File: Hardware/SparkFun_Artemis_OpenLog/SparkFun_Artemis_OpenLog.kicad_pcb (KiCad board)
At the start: 4 copper layers, 30.5 x 30.5 mm, 140 parts, among them J11 QWIIC_RIGHT_ANGLE, J14 CORTEX_JTAG, J6 MICRO-SD, Q1 20V/0.2A/8MHz/1.2Ω/1Vth, Q10 20V/0.2A/8MHz/1.2Ω/1Vth, Q2 20V/4.2A/52mΩ/1.4W, Q3 20V/0.2A/8MHz/1.2Ω/1Vth, Q7 20V/0.2A/8MHz/1.2Ω/1Vth, Q9 20V/0.2A/8MHz/1.2Ω/1Vth, U1 3.0V Supervisor, U10 CH340E, U13 9DoF IMU, U14 1.8V/100mA, U2 MCP73831, U3 3.3V, U4 3.3V, U8 ARTEMIS_MODULE, Y3 32.768kHz

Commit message: Updates the design export
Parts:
- removed C51, C52: 0.1uF, 0402-TIGHT
- removed C53, C54: 1.0uF, 0402-TIGHT
- removed Q1, Q10, Q3, Q7, Q9: 20V/0.2A/8MHz/1.2Ω/1Vth, SOT-416FL
- removed R40, R41, R44, R45, R46, R47, R48: 2.2k, 0402-TIGHT
- removed R49: DNP, 0402-TIGHT
- removed U13: 9DoF IMU, QFN24-3X3-ICM-20948
- removed U14: 1.8V/100mA, SC70
- added C10: 0.1uF, 0402, B.Cu at (161.7, 107.5)
- added C11: 0.1uF, 0402, B.Cu at (161.7, 106.0)
- added C6: 22pF, 0402-TIGHT, B.Cu at (159.6, 96.9)
- added C8: 22pF, 0402-TIGHT, B.Cu at (161.7, 96.9)
- added C9: 0.1uF, 0402, B.Cu at (159.2, 106.0)
- added R10: 4.7k, 0402-TIGHT, B.Cu at (158.9, 110.6)
- added R11: 4.7k, 0402-TIGHT, B.Cu at (158.9, 109.6)
- added R12: 100k, 0402-TIGHT, B.Cu at (161.7, 95.9)
- added R9: 100k, 0402-TIGHT, B.Cu at (158.9, 108.6)
- added U5: BNO086, LGA-28, B.Cu at (159.9, 102.5)
- added Y1: 32.768kHz, CRYSTAL-SMD-3.2X1.5MM, B.Cu at (160.7, 98.4)
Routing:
- net ICM-20948-LV_#_1.8V: track 43.4 -> 0.00 mm, vias 4 -> 0
- net ICM_PWR: track 41.5 -> 0.00 mm, vias 3 -> 0
- net SCK: track 53.8 -> 25.5 mm, vias 3 -> 2
- net ICM_~{CS}: track 34.6 -> 20.2 mm
- net S_SDA: track 0.00 -> 10.2 mm
- net N$5: track 0.00 -> 8.04 mm
- net S_SCL: track 0.00 -> 7.95 mm
- net ICM_INT: track 17.7 -> 24.1 mm, vias 1 -> 3
- net ~{RST}: track 0.00 -> 6.24 mm
- net GND: track 17.3 -> 11.8 mm, vias 35 -> 29
- net ICM-20948-LV_~{CS}: track 5.56 -> 0.00 mm
- net SDO: track 32.7 -> 27.2 mm
- net ICM-20948-LV_SDO: track 5.13 -> 0.00 mm
- net N$3: track 0.00 -> 4.71 mm
- net ICM-20948-LV_SCK: track 4.65 -> 0.00 mm
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
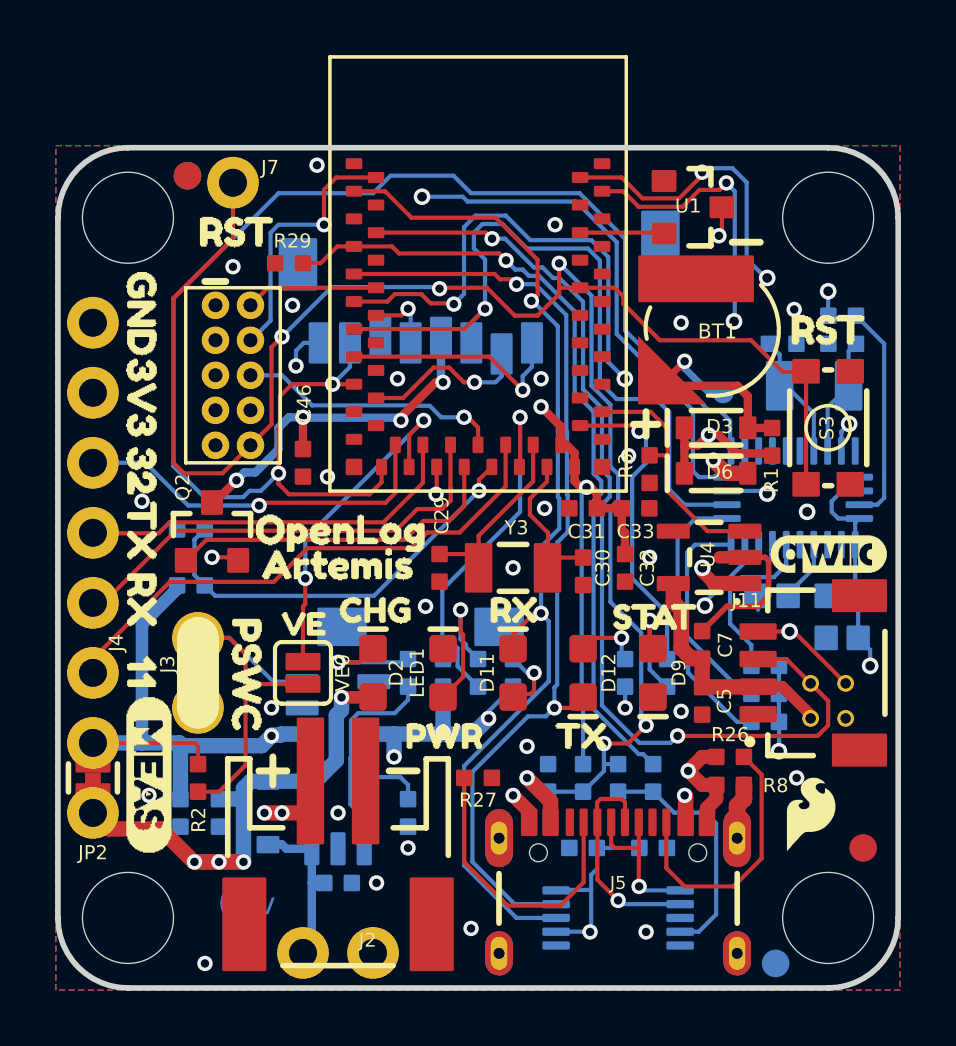
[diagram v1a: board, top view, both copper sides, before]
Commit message: Generates footprint library, updates many parts from the SparkFun KiCaad libraries
* This is just a save point
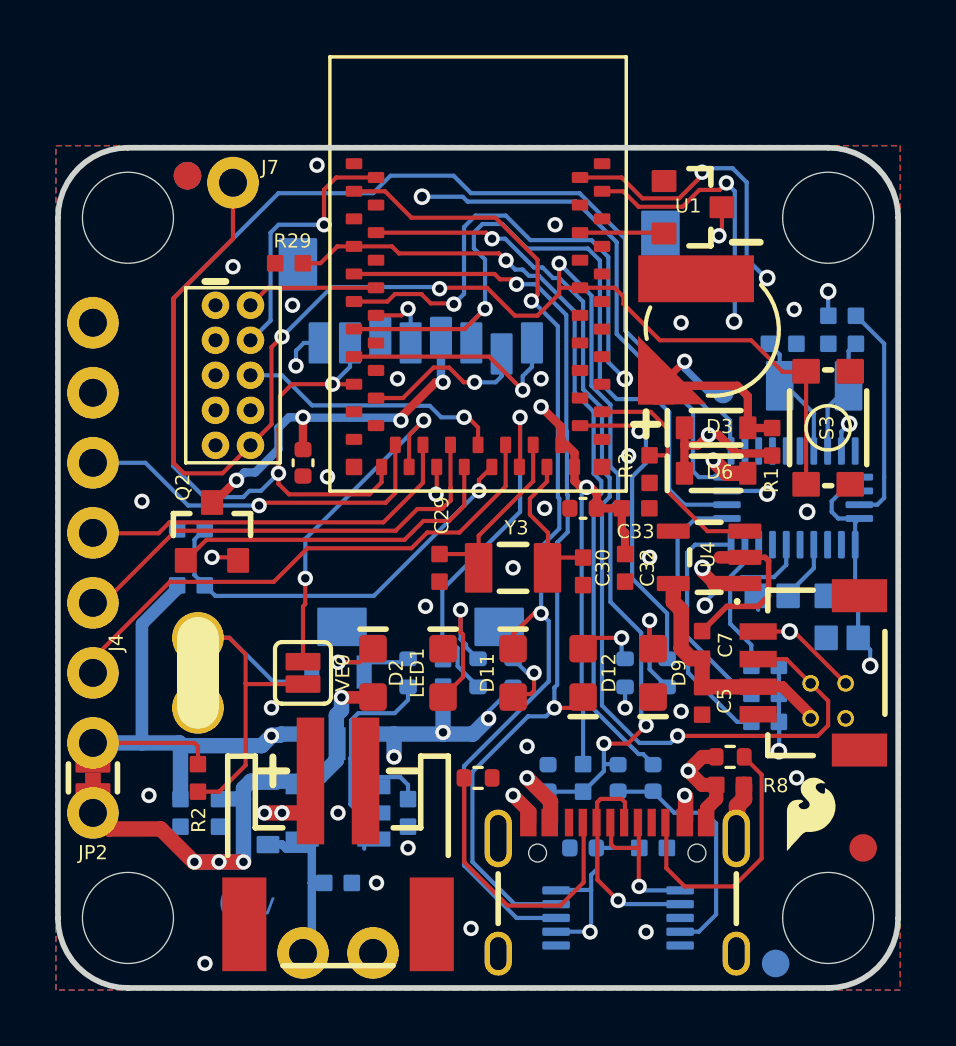
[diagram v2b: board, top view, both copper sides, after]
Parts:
- removed J1: , 1X02_NO_SILK
- removed U$1: , QWIIC#LOGO#JPG
- removed U$10, U$11: , PSWC0
- removed U$12, U$8: , RST0
- removed U$13: , C0
- removed U$14: , D0
- removed U$15: , 30
- removed U$2: , CHG2
- removed U$27: , MEAS3
- removed U$28: , OPENLOG12
- removed U$3: , PWR0
- removed U$32: , RST9
- removed U$33: , VIN8
- removed U$34, U$35: , 3V34
- removed U$36, U$37: , 113
- removed U$38, U$39: , 322
- removed U$4: , RX4
- removed U$40, U$41: , GND5
- removed U$42, U$54: , RX1
- removed U$43, U$49: , X0
- removed U$44, U$50: , Y1
- removed U$45, U$51: , Z2
- removed U$46: , G5
- removed U$47: , A4
- removed U$48: , M3
- removed U$5: , STAT5
- removed U$55, U$56: , TX0
- removed U$6: , VE0
- removed U$7: , TX3
- removed U$9: , ARTEMIS13
- added J8: USB_C_Receptacle, SparkFun-Connector:USB-C_16, F.Cu at (153.6, 113.9)
- BT1: footprint ML414H_IV01E -> SparkFun-Battery:ML414H_IV01E
- C31, C41, C42, C43, C44, C46: footprint 0402-TIGHT -> SparkFun-Capacitor:C_0402_1005Metric
- J11: value QWIIC_RIGHT_ANGLE -> Qwiic_RA; footprint JST04_1MM_RA -> SparkFun-Connector:JST_1x04_P1.0mm_Horizontal_SMD
- J2: value (none) -> Conn_01x02; footprint JST-2-SMD -> SparkFun-Connector:1x02_P2.54mm
- J3: value (none) -> Conn_01x02; footprint 1X02_NO_SILK -> SparkFun-Connector:1x02_P2.54mm
- J4: value (none) -> CONN_06NO_SILK_NO_POP
- J5: value (none) -> JST_2mm_LiPo; footprint USB-C-16P_4LAYER-PADS -> SparkFun-Connector:JST_1x02_P2.0mm_Horizontal_SMD
- J7: value (none) -> CONN_01PTH_NO_SILK_YES_STOP
- R22, R23, R24, R25, R26, R27, R5: footprint 0402-TIGHT -> SparkFun-Resistor:R_0402_1005Metric
- U2: footprint SOT23-5 -> SparkFun-Semiconductor-Standard:SOT23-5
- U3: value 3.3V -> AP2112K-3.3; footprint SOT23-5 -> SparkFun-Semiconductor-Standard:SOT23-5
- VE0: value (none) -> JUMPER-SMT_2_NO_SILK
- moved J5 10.5 mm to (143.4, 116.4), turned to 180 degrees
- moved J2 2.84 mm to (142.2, 119.0), turned to 0 degrees
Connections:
- net ARTEMIS_~{AD12/TX1} renamed ARTEMIS_~{AD12/TX1}
- net ARTEMIS_~{AD13/RX1} renamed ARTEMIS_~{AD13/RX1}
- net CHG_LED renamed Net-(U2-STAT)
- net SD_PWR renamed Net-(Q2-D)
- net S_SCL renamed Net-(U5-S_SCL)
- net S_SDA renamed Net-(U5-S_SDA)
- net VIN/3 renamed VIN/3
- net VREG_EN1 renamed Net-(U8-(SDA2/SDI2/RX1)~{D25})
- J11 pad NC1: (no net) -> unconnected-(J11-NC-PadNC1)
- J11 pad NC2: (no net) -> unconnected-(J11-NC-PadNC2)
- J2 pad 1: GND -> V_BATT
- J2 pad 2: V_BATT -> GND
- R26 pad 2: CC3 -> Net-(J8-CC2)
- R27 pad 2: CC4 -> Net-(J8-CC1)
- R8 pad 2: N$1 -> Net-(J8-SHIELD)
- U10 pad 1: D+2 -> Net-(U10-UD+)
- U10 pad 2: D-2 -> Net-(U10-UD-)
- U10 pad 5: (no net) -> unconnected-(U10-~{CTS}-Pad5)
- U10 pad 6: (no net) -> unconnected-(U10-TNOW-Pad6)
- U3 pad 4: (no net) -> unconnected-(U3-NC-Pad4)
- U4 pad 4: (no net) -> unconnected-(U4-NC-Pad4)
- U8 pad AD16: (no net) -> unconnected-(U8-AD16(TRIG0/SCCRST)-PadAD16)
- U8 pad D0: (no net) -> unconnected-(U8-(SLSCK/SLSCL/CLKOUT)D0-PadD0)
- U8 pad D1: (no net) -> unconnected-(U8-(SLSDO/SLSDA)D1-PadD1)
- U8 pad D10: (no net) -> unconnected-(U8-(SDO1/TX1/PDMCLK)D10-PadD10)
- U8 pad D14: (no net) -> unconnected-(U8-(ADCD1P/TX1/PDMCLK)D14-PadD14)
- U8 pad D17: (no net) -> unconnected-(U8-(CMPRF1/TRIG1/SCCCLK)D17-PadD17)
- U8 pad D2: (no net) -> unconnected-(U8-(SLSDI)D2-PadD2)
- U8 pad D36: (no net) -> unconnected-(U8-(RX1/TRIG1/PDMDATA)D36-PadD36)
- U8 pad D38: (no net) -> unconnected-(U8-(SDO3/RX1)D38-PadD38)
- U8 pad D40: (no net) -> unconnected-(U8-(SDA4/SDI4/RX1)D40-PadD40)
- U8 pad D41: (no net) -> unconnected-(U8-(BLEIF_IRQ/SWO/I2SWCLK)D41-PadD41)
- U8 pad ~AD31: (no net) -> unconnected-(U8-~{AD31(SCCCLK})-Pad~AD31)
- U8 pad ~AD35: (no net) -> unconnected-(U8-~{AD35(TX1/I2SDAT/PDMCLK})-Pad~AD35)
- U8 pad ~D24: (no net) -> unconnected-(U8-(TX1/32KHZ/SWO)~{D24}-Pad~D24)
- U8 pad ~D28: (no net) -> unconnected-(U8-(SDO2/I2SWCLK)~{D28}-Pad~D28)
- U8 pad ~D39: (no net) -> unconnected-(U8-(SCL4/SCK4/TX1)~{D39}-Pad~D39)
- U8 pad ~D42: (no net) -> unconnected-(U8-(SCL3/SCK3/TX1)~{D42}-Pad~D42)
- U8 pad ~D43: (no net) -> unconnected-(U8-(SDA3/SDI3/RX1)~{D43}-Pad~D43)
- U8 pad ~D45: (no net) -> unconnected-(U8-(SWO/I2SDAT/PDMDATA)~{D45}-Pad~D45)
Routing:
- net N$1: track 19.0 -> 0.00 mm
- net (no net): track 0.00 -> 17.0 mm
- net Net-(J8-CC1): track 0.00 -> 10.6 mm
- net CC4: track 10.6 -> 0.00 mm
- net Net-(J8-CC2): track 0.00 -> 9.77 mm
- net CC3: track 9.77 -> 0.00 mm
- net Net-(U10-UD-): track 0.00 -> 8.02 mm, vias 0 -> 1
- net D-2: track 8.02 -> 0.00 mm, vias 1 -> 0
- net Net-(U10-UD+): track 0.00 -> 5.74 mm, vias 0 -> 1
- net D+2: track 5.74 -> 0.00 mm, vias 1 -> 0
- net Net-(J8-SHIELD): track 0.00 -> 2.03 mm

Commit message: Another save point
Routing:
- net (no net): track 17.0 -> 21.0 mm
- net Net-(D2-PadC): track 4.05 -> 0.00 mm
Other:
- rule pad_to_mask_clearance: 0 -> 0.05

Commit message: Save spot
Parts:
- removed LED1: RED, LED-0603
- added D20: Red, SparkFun-LED:LED_0603_1608Metric_Red, F.Cu at (147.2, 108.8)
- C1, C3, C32, C33, C4, C40, C6, C8: footprint 0402-TIGHT -> SparkFun-Capacitor:C_0402_1005Metric
- C10, C11, C9: footprint 0402 -> SparkFun-Capacitor:C_0402_1005Metric
- D11, D2: footprint LED-0603 -> SparkFun-LED:LED_0603_1608Metric_Yellow
- D12: value GREEN -> Green; footprint LED-0603 -> SparkFun-LED:LED_0603_1608Metric_Green
- D9: value BLUE -> Blue; footprint LED-0603 -> SparkFun-LED:LED_0603_1608Metric_Blue
- JP2: value MEAS -> Measure; footprint COMBO-JUMPER_2_NC_TRACE -> SparkFun-Jumper:Jumper_2_PTH_SMD_Combo-NC
- Q2: value 20V/4.2A/52mΩ/1.4W -> DMG2305UX; footprint SOT23-3 -> SparkFun-Semiconductor-Standard:SOT23-3
- R1, R10, R11, R12, R28, R4, R8, R9: footprint 0402-TIGHT -> SparkFun-Resistor:R_0402_1005Metric
- R2: value 330K -> 100k; footprint 0402-TIGHT -> SparkFun-Resistor:R_0402_1005Metric
- R6: value 1M -> 100k; footprint 0402-TIGHT -> SparkFun-Resistor:R_0402_1005Metric
- R7: value 2M -> 200k; footprint 0402-TIGHT -> SparkFun-Resistor:R_0402_1005Metric
- U10: footprint MSOP10 -> SparkFun-Semiconductor-Standard:MSOP-10_3x3mm_P0.5mm
- U4: value 3.3V -> AP2112K-3.3; footprint SOT23-5 -> SparkFun-Semiconductor-Standard:SOT23-5
- turned D11 to -90 degrees
- turned D12 to 90 degrees
- turned D2 to -90 degrees
- turned D9 to 90 degrees
- turned Q2 to 90 degrees
- turned U2 to 90 degrees
- turned U3 to 0 degrees
- turned U4 to 180 degrees
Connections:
- J5 pad 1: V_BATT -> GND
- J5 pad 2: GND -> V_BATT
- R23 pad 1: Net-(D9-PadA) -> Net-(D9-A)
- R24 pad 1: Net-(D11-PadA) -> Net-(D11-A)
- R25 pad 1: Net-(D12-PadA) -> Net-(D12-A)
- R5 pad 2: Net-(D2-PadC) -> Net-(D2-K)
- U10 pad 4: ARTEMIS_~{RTS} -> unconnected-(U10-~{RTS}-Pad4)
- U10 pad 5: unconnected-(U10-~{CTS}-Pad5) -> ARTEMIS_~{RTS}
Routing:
- net (no net): track 21.0 -> 17.0 mm
- net Net-(D2-K): track 0.00 -> 4.05 mm, vias 0 -> 1
- net Net-(D9-PadA): track 3.75 -> 0.00 mm, vias 1 -> 0
- net Net-(D9-A): track 0.00 -> 3.75 mm, vias 0 -> 1
- net Net-(D11-PadA): track 2.53 -> 0.00 mm, vias 1 -> 0
- net Net-(D11-A): track 0.00 -> 2.53 mm, vias 0 -> 1
- net Net-(D12-PadA): track 2.38 -> 0.00 mm, vias 1 -> 0
- net Net-(D12-A): track 0.00 -> 2.38 mm, vias 0 -> 1
- net Net-(D2-PadC): vias 1 -> 0
